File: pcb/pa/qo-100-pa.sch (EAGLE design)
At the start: 45 parts, among them CON1 2EDG-2P, Q1 BLP9G0722-20G, U1 ADP7142AUJZ, U2 2450BP15E0100

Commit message: Lots of changes PCBs in production Stencil in production Added and changed simulation files
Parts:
- C10, C17: value 20pF -> 12pF; REF GQM1875C2E200GB12 -> (none)
- C12: REF GJM0225C1CR50BB01 -> (none)
- C13, C15: value 12pF -> 2.2pF; REF GQM1875C2E120GB12 -> (none)
- C14: REF GQM1875C2E5R6CB12 -> (none)
- C16: REF GQM1875C2E2R2BB12 -> (none)
- C18: REF GQM1875C2E1R8BB12 -> (none)
- C19, C8: value 43pF -> 47pF; REF GQM1875C2E430GB12 -> (none)
- C20, C6: REF GQM1875C2E120GB12 -> (none)
- C21, C7: value 62pF -> 100pF; REF GQM1875C2E620GB12 -> (none)
- C22: REF GQM1875C2E1R2BB12 -> (none)
- F1: TRIP 4A -> 3.5A

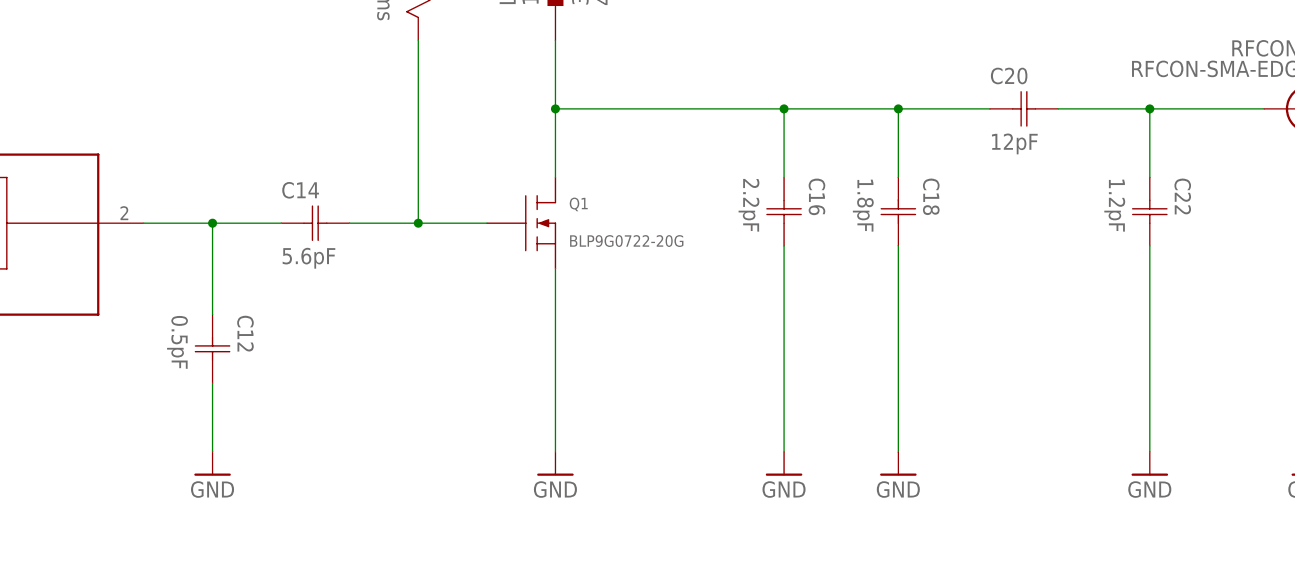
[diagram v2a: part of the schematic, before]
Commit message: Matched PA to 2.4 GHz
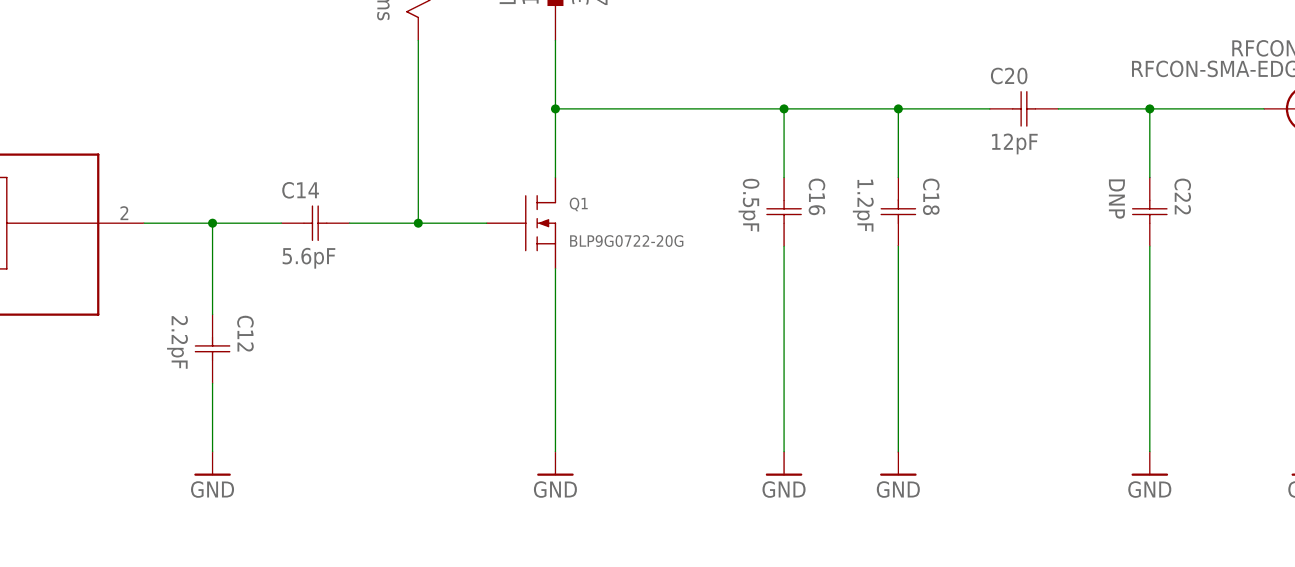
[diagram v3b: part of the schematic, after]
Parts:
- C12: value 0.5pF -> 2.2pF
- C16: value 2.2pF -> 0.5pF
- C18: value 1.8pF -> 1.2pF
- C22: value 1.2pF -> DNP
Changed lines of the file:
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@@
 <part name="Q1" library="Ampleon" deviceset="BLP9G0722-20" device="G"/>
 <part name="RFCON1" library="RF Connector" deviceset="RFCON" device="-SMA-EDGE"/>
-<part name="C12" library="Capacitor" deviceset="CAPACITOR" device="-0603" value="0.5pF"/>
+<part name="C12" library="Capacitor" deviceset="CAPACITOR" device="-0603" value="2.2pF"/>
 <part name="GND1" library="Supply Symbol" deviceset="GND" device=""/>
 <part name="GND2" library="Supply Symbol" deviceset="GND" device=""/>
 <part name="C14" library="Capacitor" deviceset="CAPACITOR" device="-0603" value="5.6pF"/>
-<part name="C16" library="Capacitor" deviceset="CAPACITOR" device="-0603" value="2.2pF"/>
-<part name="C18" library="Capacitor" deviceset="CAPACITOR" device="-0603" value="1.8pF"/>
-<part name="C22" library="Capacitor" deviceset="CAPACITOR" device="-0603" value="1.2pF"/>
+<part name="C16" library="Capacitor" deviceset="CAPACITOR" device="-0603" value="0.5pF"/>
+<part name="C18" library="Capacitor" deviceset="CAPACITOR" device="-0603" value="1.2pF"/>
+<part name="C22" library="Capacitor" deviceset="CAPACITOR" device="-0603" value="DNP"/>
 <part name="C20" library="Capacitor" deviceset="CAPACITOR" device="-0603" value="12pF"/>
 <part name="GND3" library="Supply Symbol" deviceset="GND" device=""/>

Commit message: Update 2EDG library on PA
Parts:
- CON1: value 2EDG-2P -> 2EDG-2P-5.08MM; device Generic Connector:2EDG-2P -> Generic Connector:2EDG-2P-5.08MM
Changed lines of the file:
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@@
 </part>
 <part name="GND22" library="Supply Symbol" deviceset="GND" device=""/>
-<part name="CON1" library="Generic Connector" deviceset="2EDG-2P" device=""/>
+<part name="CON1" library="Generic Connector" deviceset="2EDG-2P" device="-5.08MM"/>
 <part name="GND23" library="Supply Symbol" deviceset="GND" device=""/>
 <part name="VCC6" library="Supply Symbol" deviceset="VDD" device=""/>
